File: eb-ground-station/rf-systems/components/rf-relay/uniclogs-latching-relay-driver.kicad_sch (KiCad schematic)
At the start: 5 parts, among them J1 Conn_01x05

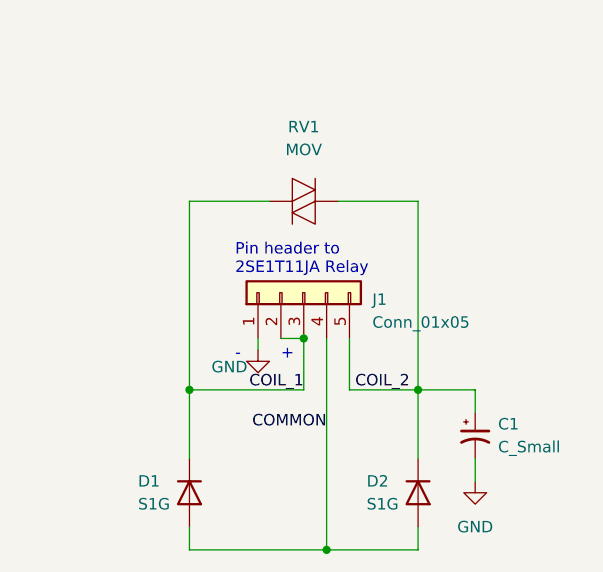
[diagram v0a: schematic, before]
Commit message: modified schematic diagram for clarity
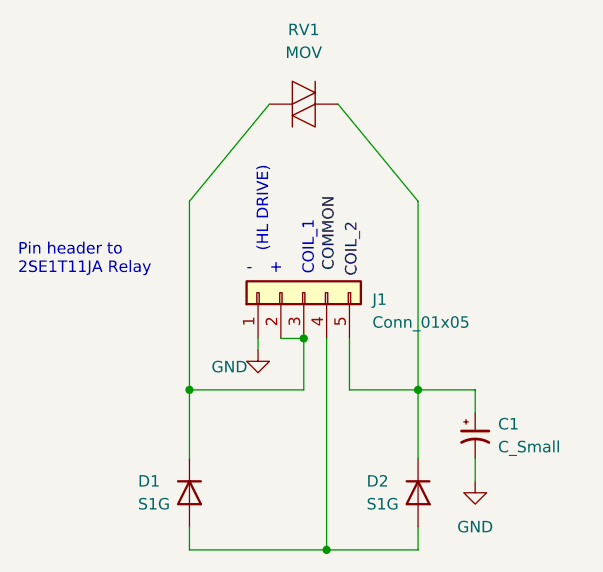
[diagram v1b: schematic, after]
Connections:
- net COIL_2: no longer C1.1, D2.1 (K), J1.5 (Pin_5), RV1.2
- net COMMON: no longer D1.2 (A), D2.2 (A), J1.4 (Pin_4)
- net COIL_1 renamed  
- new net: D1.2 (A), D2.2 (A), J1.4 (Pin_4)
- new net: C1.1, D2.1 (K), J1.5 (Pin_5), RV1.2
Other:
- note added: "(HL DRIVE)"
- note added: "COIL_1"
- moved on the sheet: RV1
